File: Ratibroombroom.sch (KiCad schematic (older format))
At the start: 112 parts, among them J1 Conn_01x02_Male, J10 Conn_01x04_Male, J11 Conn_01x04_Male, J2 Conn_01x02_Male, J3 Conn_01x10_Male, J5 Conn_01x02_Male, J6 Conn_01x02_Male, J8 Conn_01x04_Male, J9 Conn_01x04_Male, Q1 IRLML6344, Q10 S8050, Q11 IRF7416PbF, Q2 IRLML6344, Q3 IRLML6344, Q4 IRLML6344, Q5 PT12-21B/TR8, Q6 PT12-21B/TR8, Q7 PT12-21B/TR8, Q8 PT12-21B/TR8, Q9 IRLML6344, SW1 B3U, SW2 B3U, SW3 PCM12, U1 AZ1117-3.3, U2 DRV8835, U3 AS5145B-HSST, U4 MPU-9250, U5 STM32F405RGTx, U6 AS5145B-HSST, U7 DRV8835, U8 L6932D1.2TR, U9 L6932D1.2TR, Y1 8MHZ

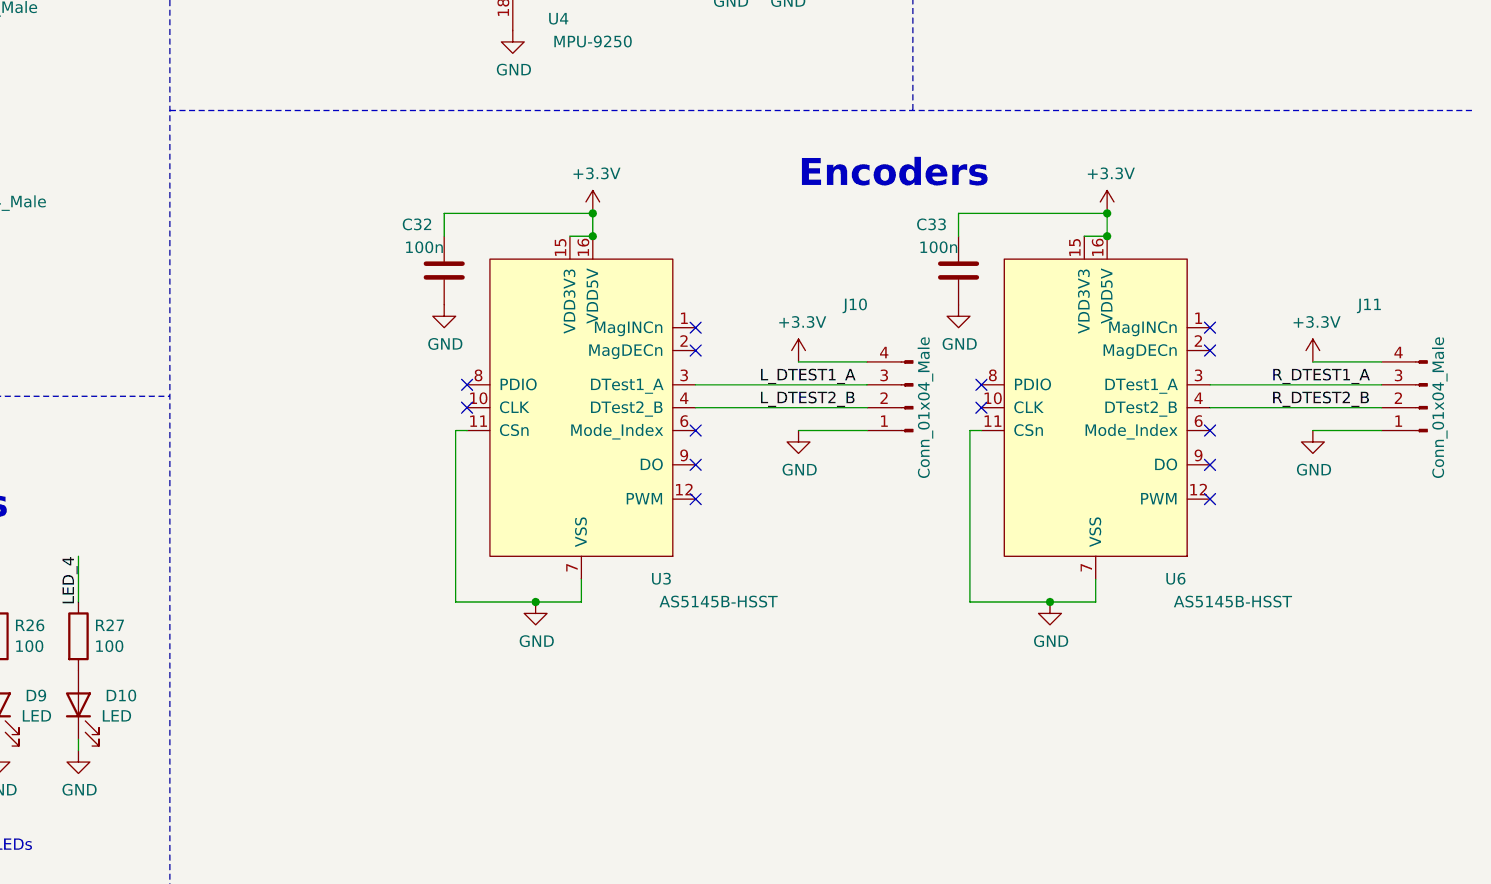
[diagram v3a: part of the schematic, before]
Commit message: Change encoder board connectors so that the boards will be rotated in the final assembly. Add separate ground and power nets to encoder boards to pass DRC cleanly. Add some logos
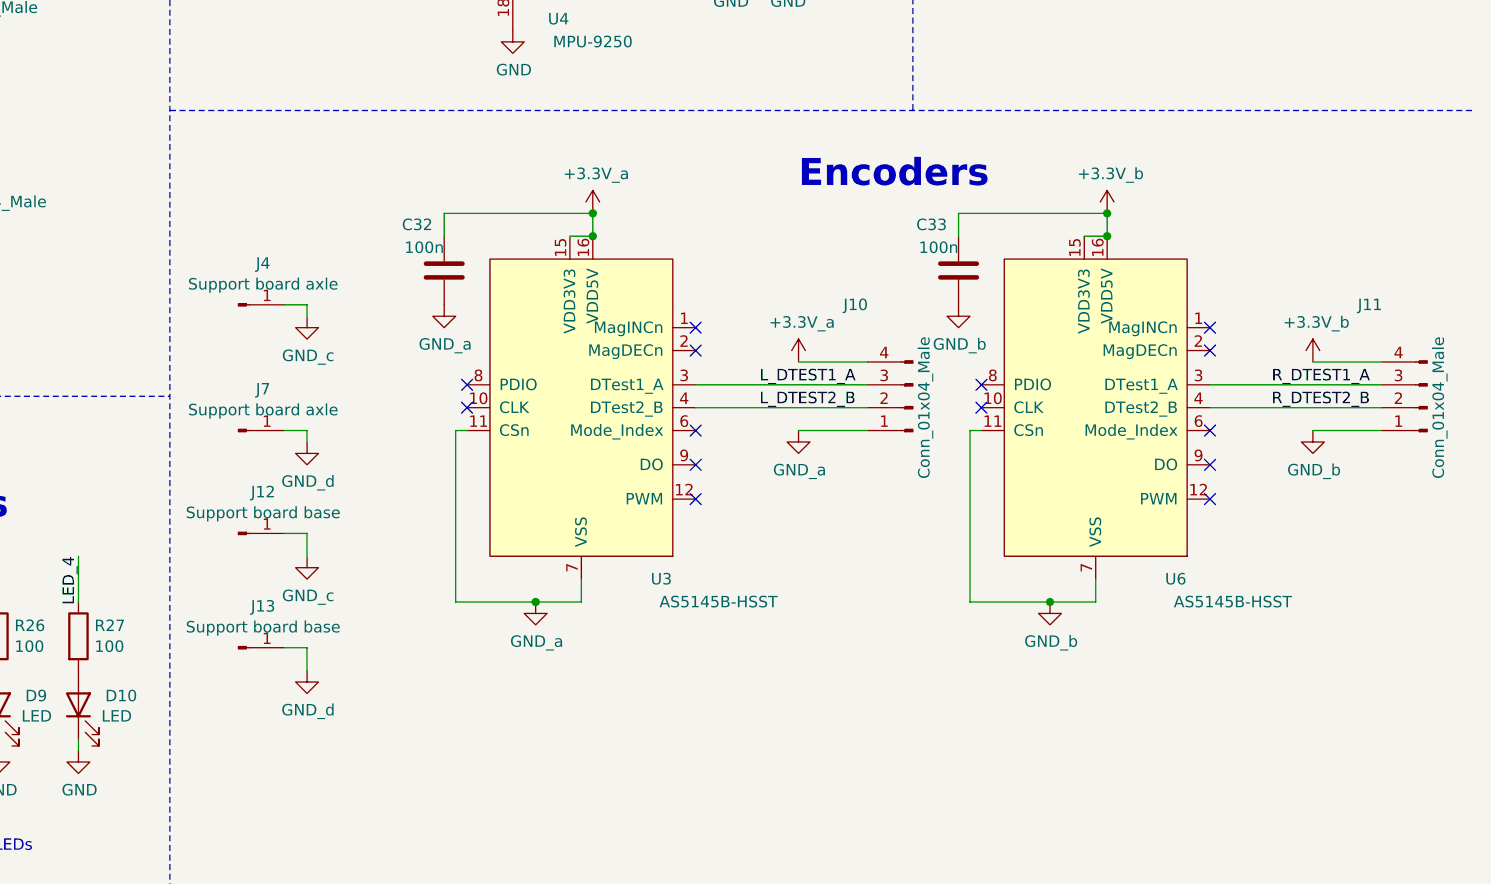
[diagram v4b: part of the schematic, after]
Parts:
- added J12, J13: Support board base, Ratibroombroom:Encoder_base_connector, symbol Connector:Conn_01x01_Male
- added J4, J7: Support board axle, Ratibroombroom:Encoder_axle_hole, symbol Connector:Conn_01x01_Male
- J10, J11: footprint Ratibroombroom:Pad_SMD_4P_1x3mm -> Ratibroombroom:Pad_SMD_4P_1x1.5mm
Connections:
- net labels added: +3.3V_a, +3.3V_b, GND_a, GND_b, GND_c, GND_d
- wire segments 417 -> 425
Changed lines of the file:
@@
 	7750 6450 8250 6450
 $Comp
-L power:GND #PWR0109
+L schematic_sybmols:GND_a #PWR0109
 U 1 1 5F3B96E6
 P 11950 9600
 F 0 "#PWR0109" H 11950 9350 50  0001 C CNN
-F 1 "GND" H 11955 9427 50  0000 C CNN
+F 1 "GND_a" H 11955 9427 50  0000 C CNN
 F 2 "" H 11950 9600 50  0001 C CNN
 F 3 "" H 11950 9600 50  0001 C CNN
@@
 	11950 9600 11600 9600
 $Comp
-L power:+3.3V #PWR0110
+L schematic_sybmols:+3.3V_a #PWR0110
 U 1 1 5F3DA58B
 P 12200 7900
 F 0 "#PWR0110" H 12200 7750 50  0001 C CNN
-F 1 "+3.3V" H 12215 8073 50  0000 C CNN
+F 1 "+3.3V_a" H 12215 8073 50  0000 C CNN
 F 2 "" H 12200 7900 50  0001 C CNN
 F 3 "" H 12200 7900 50  0001 C CNN
@@
 F 0 "J10" H 13850 8300 50  0000 C CNN
 F 1 "Conn_01x04_Male" V 13550 8750 50  0000 C CNN
-F 2 "Ratibroombroom:Pad_SMD_4P_1x3mm" H 13600 8750 50  0001 C CNN
+F 2 "Ratibroombroom:Pad_SMD_4P_1x1.5mm" H 13600 8750 50  0001 C CNN
 F 3 "~" H 13600 8750 50  0001 C CNN
 	1    13600 8750
@@
 $EndComp
 $Comp
-L power:GND #PWR0111
+L schematic_sybmols:GND_a #PWR0111
 U 1 1 5F4BE553
 P 13100 8850
 F 0 "#PWR0111" H 13100 8600 50  0001 C CNN
-F 1 "GND" H 13105 8677 50  0000 C CNN
+F 1 "GND_a" H 13105 8677 50  0000 C CNN
 F 2 "" H 13100 8850 50  0001 C CNN
 F 3 "" H 13100 8850 50  0001 C CNN
@@
 Text Label 13350 8650 2    50   ~ 0
 L_DTEST1_A
-$Comp
-L power:+3.3V #PWR0112
-U 1 1 5F4BE562
-P 13100 8550
-F 0 "#PWR0112" H 13100 8400 50  0001 C CNN
-F 1 "+3.3V" H 13115 8723 50  0000 C CNN
-F 2 "" H 13100 8550 50  0001 C CNN
-F 3 "" H 13100 8550 50  0001 C CNN
-	1    13100 8550
-	1    0    0    -1
-$EndComp
 Wire Wire Line
 	13400 8550 13100 8550
@@
 R_ENCODER_B
 $Comp
-L power:GND #PWR0117
+L schematic_sybmols:GND_b #PWR0117
 U 1 1 5F6A86DD
 P 14200 9600
 F 0 "#PWR0117" H 14200 9350 50  0001 C CNN
-F 1 "GND" H 14205 9427 50  0000 C CNN
+F 1 "GND_b" H 14205 9427 50  0000 C CNN
 F 2 "" H 14200 9600 50  0001 C CNN
 F 3 "" H 14200 9600 50  0001 C CNN
@@
 Wire Wire Line
 	14200 9600 13850 9600
-$Comp
-L power:+3.3V #PWR0118
-U 1 1 5F6A86ED
-P 14450 7900
-F 0 "#PWR0118" H 14450 7750 50  0001 C CNN
-F 1 "+3.3V" H 14465 8073 50  0000 C CNN
-F 2 "" H 14450 7900 50  0001 C CNN
-F 3 "" H 14450 7900 50  0001 C CNN
-	1    14450 7900
-	1    0    0    -1
-$EndComp
 Wire Wire Line
 	14450 7900 14450 8000
@@
 F 0 "J11" H 16100 8300 50  0000 C CNN
 F 1 "Conn_01x04_Male" V 15800 8750 50  0000 C CNN
-F 2 "Ratibroombroom:Pad_SMD_4P_1x3mm" H 15850 8750 50  0001 C CNN
+F 2 "Ratibroombroom:Pad_SMD_4P_1x1.5mm" H 15850 8750 50  0001 C CNN
 F 3 "~" H 15850 8750 50  0001 C CNN
 	1    15850 8750
@@
 $EndComp
 $Comp
-L power:GND #PWR0119
+L schematic_sybmols:GND_b #PWR0119
 U 1 1 5F6A870B
 P 15350 8850
 F 0 "#PWR0119" H 15350 8600 50  0001 C CNN
-F 1 "GND" H 15355 8677 50  0000 C CNN
+F 1 "GND_b" H 15355 8677 50  0000 C CNN
 F 2 "" H 15350 8850 50  0001 C CNN
 F 3 "" H 15350 8850 50  0001 C CNN
@@
 Wire Wire Line
 	15650 8650 14900 8650
-$Comp
-L power:+3.3V #PWR0120
-U 1 1 5F6A8719
-P 15350 8550
-F 0 "#PWR0120" H 15350 8400 50  0001 C CNN
-F 1 "+3.3V" H 15365 8723 50  0000 C CNN
-F 2 "" H 15350 8550 50  0001 C CNN
-F 3 "" H 15350 8550 50  0001 C CNN
-	1    15350 8550
-	1    0    0    -1
-$EndComp
 Wire Wire Line
 	15650 8550 15350 8550
@@
 Connection ~ 12200 8000
 $Comp
-L power:GND #PWR055
+L schematic_sybmols:GND_a #PWR055
 U 1 1 5E2BB3B5
 P 11550 8300
 F 0 "#PWR055" H 11550 8050 50  0001 C CNN
-F 1 "GND" H 11555 8127 50  0000 C CNN
+F 1 "GND_a" H 11555 8127 50  0000 C CNN
 F 2 "" H 11550 8300 50  0001 C CNN
 F 3 "" H 11550 8300 50  0001 C CNN
@@
 Connection ~ 12200 7900
 $Comp
-L power:GND #PWR094
+L schematic_sybmols:GND_b #PWR094
 U 1 1 5E3254D3
 P 13800 8300
 F 0 "#PWR094" H 13800 8050 50  0001 C CNN
-F 1 "GND" H 13805 8127 50  0000 C CNN
+F 1 "GND_b" H 13805 8127 50  0000 C CNN
 F 2 "" H 13800 8300 50  0001 C CNN
 F 3 "" H 13800 8300 50  0001 C CNN
@@
 Wire Wire Line
 	13800 7900 14450 7900
-Connection ~ 14450 7900
 $Comp
 L schematic_sybmols:DRV8835 U7
@@
 Wire Wire Line
 	7750 6250 8350 6250
+$Comp
+L schematic_sybmols:+3.3V_a #PWR0102
+U 1 1 5F8D2BC4
+P 13100 8550
+F 0 "#PWR0102" H 13100 8400 50  0001 C CNN
+F 1 "+3.3V_a" H 13115 8723 50  0000 C CNN
+F 2 "" H 13100 8550 50  0001 C CNN
+F 3 "" H 13100 8550 50  0001 C CNN
+	1    13100 8550
+	1    0    0    -1
+$EndComp
+$Comp
+L schematic_sybmols:+3.3V_b #PWR0103
+U 1 1 5F8D5521
+P 15350 8550
+F 0 "#PWR0103" H 15350 8400 50  0001 C CNN
+F 1 "+3.3V_b" H 15365 8723 50  0000 C CNN
+F 2 "" H 15350 8550 50  0001 C CNN
+F 3 "" H 15350 8550 50  0001 C CNN
+	1    15350 8550
+	1    0    0    -1
+$EndComp
+$Comp
+L schematic_sybmols:+3.3V_b #PWR0104
+U 1 1 5F93D32E
+P 14450 7900
+F 0 "#PWR0104" H 14450 7750 50  0001 C CNN
+F 1 "+3.3V_b" H 14465 8073 50  0000 C CNN
+F 2 "" H 14450 7900 50  0001 C CNN
+F 3 "" H 14450 7900 50  0001 C CNN
+	1    14450 7900
+	1    0    0    -1
+$EndComp
+Connection ~ 14450 7900
+$Comp
+L Connector:Conn_01x01_Male J4
+U 1 1 5F8B5004
+P 10650 8300
+F 0 "J4" H 10758 8481 50  0000 C CNN
+F 1 "Support board axle" H 10758 8390 50  0000 C CNN
+F 2 "Ratibroombroom:Encoder_axle_hole" H 10650 8300 50  0001 C CNN
+F 3 "~" H 10650 8300 50  0001 C CNN
+	1    10650 8300
+	1    0    0    -1
+$EndComp
+$Comp
+L Connector:Conn_01x01_Male J7
+U 1 1 5F8B687E
+P 10650 8850
+F 0 "J7" H 10758 9031 50  0000 C CNN
+F 1 "Support board axle" H 10758 8940 50  0000 C CNN
+F 2 "Ratibroombroom:Encoder_axle_hole" H 10650 8850 50  0001 C CNN
+F 3 "~" H 10650 8850 50  0001 C CNN
+	1    10650 8850
+	1    0    0    -1
+$EndComp
+$Comp
+L schematic_sybmols:GND_c #PWR0112
+U 1 1 5F8B9641
+P 10950 8350
+F 0 "#PWR0112" H 10950 8100 50  0001 C CNN
+F 1 "GND_c" H 10955 8177 50  0000 C CNN
+F 2 "" H 10950 8350 50  0001 C CNN
+F 3 "" H 10950 8350 50  0001 C CNN
+	1    10950 8350
+	1    0    0    -1
+$EndComp
+Wire Wire Line
+	10850 8300 10950 8300
+Wire Wire Line
+	10950 8300 10950 8350
+$Comp
+L schematic_sybmols:GND_d #PWR0118
+U 1 1 5F91DE9E
+P 10950 8900
+F 0 "#PWR0118" H 10950 8650 50  0001 C CNN
+F 1 "GND_d" H 10955 8727 50  0000 C CNN
+F 2 "" H 10950 8900 50  0001 C CNN
+F 3 "" H 10950 8900 50  0001 C CNN
+	1    10950 8900
+	1    0    0    -1
+$EndComp
+Wire Wire Line
+	10850 8850 10950 8850
+Wire Wire Line
+	10950 8850 10950 8900
+$Comp
+L Connector:Conn_01x01_Male J12
+U 1 1 5F970230
+P 10650 9300
+F 0 "J12" H 10758 9481 50  0000 C CNN
+F 1 "Support board base" H 10758 9390 50  0000 C CNN
+F 2 "Ratibroombroom:Encoder_base_connector" H 10650 9300 50  0001 C CNN
+F 3 "~" H 10650 9300 50  0001 C CNN
+	1    10650 9300
+	1    0    0    -1
+$EndComp
+$Comp
+L schematic_sybmols:GND_c #PWR0120
+U 1 1 5F97DE96
+P 10950 9400
+F 0 "#PWR0120" H 10950 9150 50  0001 C CNN
+F 1 "GND_c" H 10955 9227 50  0000 C CNN
+F 2 "" H 10950 9400 50  0001 C CNN
+F 3 "" H 10950 9400 50  0001 C CNN
+	1    10950 9400
+	1    0    0    -1
+$EndComp
+$Comp
+L Connector:Conn_01x01_Male J13
+U 1 1 5F9B682D
+P 10650 9800
+F 0 "J13" H 10758 9981 50  0000 C CNN
+F 1 "Support board base" H 10758 9890 50  0000 C CNN
+F 2 "Ratibroombroom:Encoder_base_connector" H 10650 9800 50  0001 C CNN
+F 3 "~" H 10650 9800 50  0001 C CNN
+	1    10650 9800
+	1    0    0    -1
+$EndComp
+$Comp
+L schematic_sybmols:GND_d #PWR0121
+U 1 1 5F9B743C
+P 10950 9900
+F 0 "#PWR0121" H 10950 9650 50  0001 C CNN
+F 1 "GND_d" H 10955 9727 50  0000 C CNN
+F 2 "" H 10950 9900 50  0001 C CNN
+F 3 "" H 10950 9900 50  0001 C CNN
+	1    10950 9900
+	1    0    0    -1
+$EndComp
+Wire Wire Line
+	10950 9900 10950 9800
+Wire Wire Line
+	10950 9800 10850 9800
+Wire Wire Line
+	10950 9400 10950 9300
+Wire Wire Line
+	10950 9300 10850 9300
 $EndSCHEMATC
